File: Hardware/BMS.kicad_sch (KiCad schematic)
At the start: 25 parts, among them J5 vcc, J6 gnd, U5 BQ51050BRHL

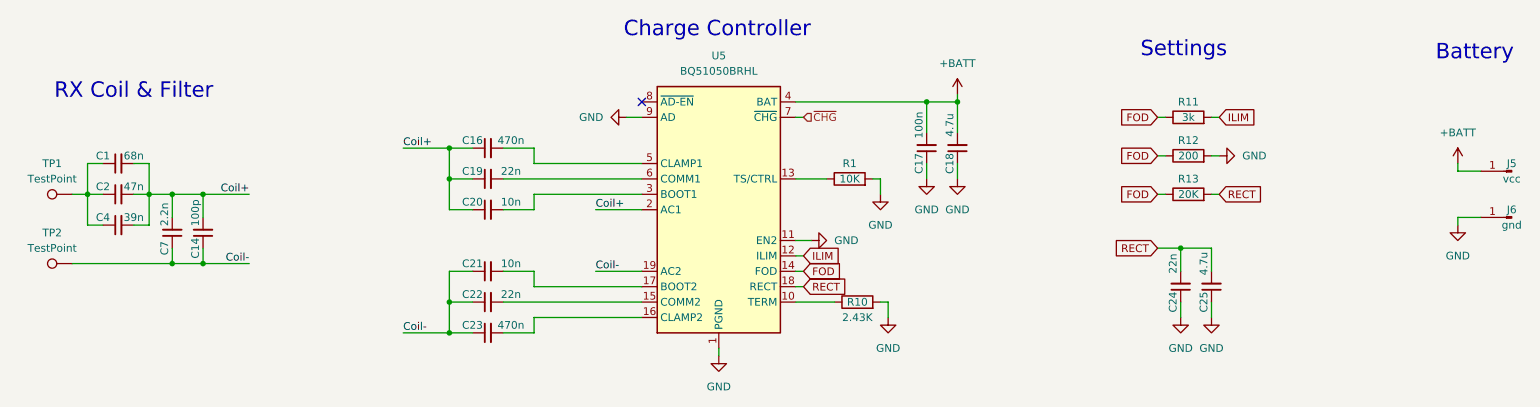
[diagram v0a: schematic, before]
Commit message: semi-final component placements and final component selections. Abandoning due to high routing complexity and need for a 4L board.
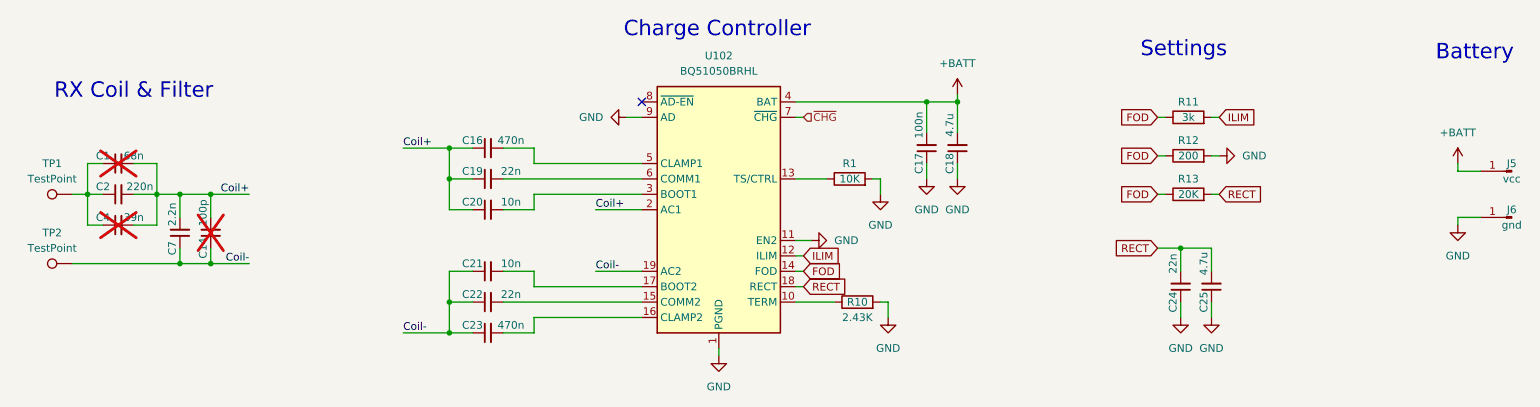
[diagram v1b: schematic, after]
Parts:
- C1, C14, C4: footprint Capacitor_SMD:C_0402_1005Metric -> LED_Custom:SMD_0402-2; now not fitted
- C16, C17, C19, C20, C21, C22, C23, C24, C7: footprint Capacitor_SMD:C_0402_1005Metric -> LED_Custom:SMD_0402-2
- C18, C25: footprint Capacitor_SMD:C_0603_1608Metric -> LED_Custom:LED_0603-2
- C2: value 47n -> 220n; footprint Capacitor_SMD:C_0402_1005Metric -> LED_Custom:SMD_0402-2
- R1, R10, R11, R12, R13: footprint Resistor_SMD:R_0402_1005Metric -> LED_Custom:SMD_0402-2
- TP1, TP2: footprint TestPoint:TestPoint_Loop_D1.80mm_Drill1.0mm_Beaded -> TestPoint:TestPoint_Pad_D1.0mm
- renumbered U5 to U102
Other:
- moved on the sheet: C7
